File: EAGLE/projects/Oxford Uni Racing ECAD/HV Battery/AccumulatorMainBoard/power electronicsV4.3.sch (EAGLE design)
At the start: 94 parts, among them IC1 4043D, IC2 SE555D, IC9 4011D, K2 T9AS5D12-12=T9A, K3 T9AS1D12-48=T9A, K6 T9AS1D12-48=T9A, K7 T9AS1D12-48=T9A, Q1 BSS138, Q2 BSS138, Q3 BSS138, Q4 BSS138

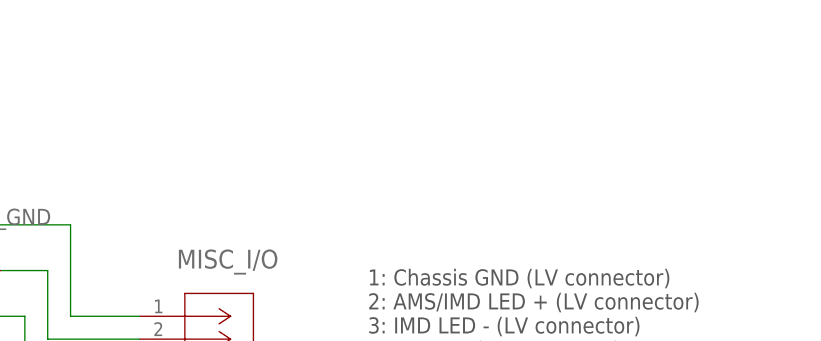
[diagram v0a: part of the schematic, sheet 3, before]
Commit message: main board schematic update with new connectors
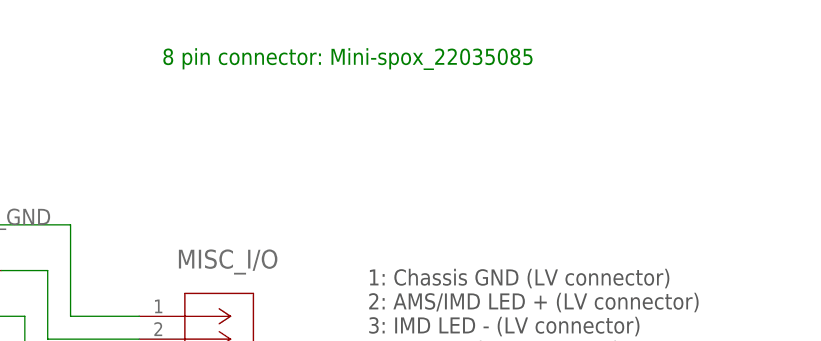
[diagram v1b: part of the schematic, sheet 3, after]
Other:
- note added: "8 pin connector: Mini-spox_22035085"
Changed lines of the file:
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@@
 <grid distance="0.1" unitdist="inch" unit="inch" style="lines" multiple="1" display="no" altdistance="0.01" altunitdist="inch" altunit="inch"/>
 <layers>
-<layer number="1" name="Top" color="4" fill="1" visible="yes" active="no"/>
-<layer number="2" name="Route2" color="16" fill="1" visible="yes" active="no"/>
-<layer number="3" name="Route3" color="17" fill="1" visible="yes" active="no"/>
-<layer number="4" name="Route4" color="18" fill="1" visible="yes" active="no"/>
-<layer number="5" name="Route5" color="19" fill="1" visible="yes" active="no"/>
-<layer number="6" name="Route6" color="25" fill="1" visible="yes" active="no"/>
-<layer number="7" name="Route7" color="26" fill="1" visible="yes" active="no"/>
-<layer number="8" name="Route8" color="27" fill="1" visible="yes" active="no"/>
-<layer number="9" name="Route9" color="28" fill="1" visible="yes" active="no"/>
-<layer number="10" name="Route10" color="29" fill="1" visible="yes" active="no"/>
-<layer number="11" name="Route11" color="30" fill="1" visible="yes" active="no"/>
-<layer number="12" name="Route12" color="20" fill="1" visible="yes" active="no"/>
-<layer number="13" name="Route13" color="21" fill="1" visible="yes" active="no"/>
-<layer number="14" name="Route14" color="22" fill="1" visible="yes" active="no"/>
-<layer number="15" name="Route15" color="23" fill="1" visible="yes" active="no"/>
-<layer number="16" name="Bottom" color="1" fill="1" visible="yes" active="no"/>
-<layer number="17" name="Pads" color="2" fill="1" visible="yes" active="no"/>
-<layer number="18" name="Vias" color="2" fill="1" visible="yes" active="no"/>
-<layer number="19" name="Unrouted" color="6" fill="1" visible="yes" active="no"/>
-<layer number="20" name="Dimension" color="24" fill="1" visible="yes" active="no"/>
-<layer number="21" name="tPlace" color="7" fill="1" visible="yes" active="no"/>
-<layer number="22" name="bPlace" color="7" fill="1" visible="yes" active="no"/>
-<layer number="23" name="tOrigins" color="15" fill="1" visible="yes" active="no"/>
-<layer number="24" name="bOrigins" color="15" fill="1" visible="yes" active="no"/>
-<layer number="25" name="tNames" color="7" fill="1" visible="yes" active="no"/>
-<layer number="26" name="bNames" color="7" fill="1" visible="yes" active="no"/>
-<layer number="27" name="tValues" color="7" fill="1" visible="yes" active="no"/>
-<layer number="28" name="bValues" color="7" fill="1" visible="yes" active="no"/>
+<layer number="1" name="Top" color="4" fill="1" visible="no" active="no"/>
+<layer number="2" name="Route2" color="16" fill="1" visible="no" active="no"/>
+<layer number="3" name="Route3" color="17" fill="1" visible="no" active="no"/>
+<layer number="4" name="Route4" color="18" fill="1" visible="no" active="no"/>
+<layer number="5" name="Route5" color="19" fill="1" visible="no" active="no"/>
+<layer number="6" name="Route6" color="25" fill="1" visible="no" active="no"/>
+<layer number="7" name="Route7" color="26" fill="1" visible="no" active="no"/>
+<layer number="8" name="Route8" color="27" fill="1" visible="no" active="no"/>
+<layer number="9" name="Route9" color="28" fill="1" visible="no" active="no"/>
+<layer number="10" name="Route10" color="29" fill="1" visible="no" active="no"/>
+<layer number="11" name="Route11" color="30" fill="1" visible="no" active="no"/>
+<layer number="12" name="Route12" color="20" fill="1" visible="no" active="no"/>
+<layer number="13" name="Route13" color="21" fill="1" visible="no" active="no"/>
+<layer number="14" name="Route14" color="22" fill="1" visible="no" active="no"/>
+<layer number="15" name="Route15" color="23" fill="1" visible="no" active="no"/>
+<layer number="16" name="Bottom" color="1" fill="1" visible="no" active="no"/>
+<layer number="17" name="Pads" color="2" fill="1" visible="no" active="no"/>
+<layer number="18" name="Vias" color="2" fill="1" visible="no" active="no"/>
+<layer number="19" name="Unrouted" color="6" fill="1" visible="no" active="no"/>
+<layer number="20" name="Dimension" color="24" fill="1" visible="no" active="no"/>
+<layer number="21" name="tPlace" color="7" fill="1" visible="no" active="no"/>
+<layer number="22" name="bPlace" color="7" fill="1" visible="no" active="no"/>
+<layer number="23" name="tOrigins" color="15" fill="1" visible="no" active="no"/>
+<layer number="24" name="bOrigins" color="15" fill="1" visible="no" active="no"/>
+<layer number="25" name="tNames" color="7" fill="1" visible="no" active="no"/>
+<layer number="26" name="bNames" color="7" fill="1" visible="no" active="no"/>
+<layer number="27" name="tValues" color="7" fill="1" visible="no" active="no"/>
+<layer number="28" name="bValues" color="7" fill="1" visible="no" active="no"/>
 <layer number="29" name="tStop" color="7" fill="3" visible="no" active="no"/>
 <layer number="30" name="bStop" color="7" fill="6" visible="no" active="no"/>
@@
 <layer number="35" name="tGlue" color="7" fill="4" visible="no" active="no"/>
 <layer number="36" name="bGlue" color="7" fill="5" visible="no" active="no"/>
-<layer number="37" name="tTest" color="7" fill="1" visible="yes" active="no"/>
-<layer number="38" name="bTest" color="7" fill="1" visible="yes" active="no"/>
+<layer number="37" name="tTest" color="7" fill="1" visible="no" active="no"/>
+<layer number="38" name="bTest" color="7" fill="1" visible="no" active="no"/>
 <layer number="39" name="tKeepout" color="4" fill="11" visible="no" active="no"/>
 <layer number="40" name="bKeepout" color="1" fill="11" visible="no" active="no"/>
@@
 <layer number="44" name="Drills" color="7" fill="1" visible="no" active="no"/>
 <layer number="45" name="Holes" color="7" fill="1" visible="no" active="no"/>
-<layer number="46" name="Milling" color="3" fill="1" visible="yes" active="no"/>
-<layer number="47" name="Measures" color="7" fill="1" visible="yes" active="no"/>
-<layer number="48" name="Document" color="7" fill="1" visible="yes" active="no"/>
-<layer number="49" name="Reference" color="7" fill="1" visible="yes" active="no"/>
-<layer number="50" name="dxf" color="7" fill="1" visible="yes" active="no"/>
-<layer number="51" name="tDocu" color="7" fill="1" visible="yes" active="no"/>
-<layer number="52" name="bDocu" color="7" fill="1" visible="yes" active="no"/>
-<layer number="53" name="tGND_GNDA" color="7" fill="9" visible="yes" active="no"/>
-<layer number="54" name="bGND_GNDA" color="1" fill="9" visible="yes" active="no"/>
-<layer number="56" name="wert" color="7" fill="1" visible="yes" active="no"/>
-<layer number="57" name="tCAD" color="7" fill="1" visible="yes" active="no"/>
-<layer number="59" name="tCarbon" color="7" fill="1" visible="yes" active="no"/>
-<layer number="60" name="bCarbon" color="7" fill="1" visible="yes" active="no"/>
+<layer number="46" name="Milling" color="3" fill="1" visible="no" active="no"/>
+<layer number="47" name="Measures" color="7" fill="1" visible="no" active="no"/>
+<layer number="48" name="Document" color="7" fill="1" visible="no" active="no"/>
+<layer number="49" name="Reference" color="7" fill="1" visible="no" active="no"/>
+<layer number="50" name="dxf" color="7" fill="1" visible="no" active="no"/>
+<layer number="51" name="tDocu" color="7" fill="1" visible="no" active="no"/>
+<layer number="52" name="bDocu" color="7" fill="1" visible="no" active="no"/>
+<layer number="53" name="tGND_GNDA" color="7" fill="9" visible="no" active="no"/>
+<layer number="54" name="bGND_GNDA" color="1" fill="9" visible="no" active="no"/>
+<layer number="56" name="wert" color="7" fill="1" visible="no" active="no"/>
+<layer number="57" name="tCAD" color="7" fill="1" visible="no" active="no"/>
+<layer number="59" name="tCarbon" color="7" fill="1" visible="no" active="no"/>
+<layer number="60" name="bCarbon" color="7" fill="1" visible="no" active="no"/>
 <layer number="88" name="SimResults" color="9" fill="1" visible="yes" active="yes"/>
 <layer number="89" name="SimProbes" color="9" fill="1" visible="yes" active="yes"/>
@@
 3: GND (LV connector)</text>
 <text x="215.9" y="63.5" size="1.778" layer="91">CAN D-sub connector</text>
+<text x="195.58" y="243.84" size="1.778" layer="91">8 pin connector: Mini-spox_22035085</text>
 </plain>
 <instances>

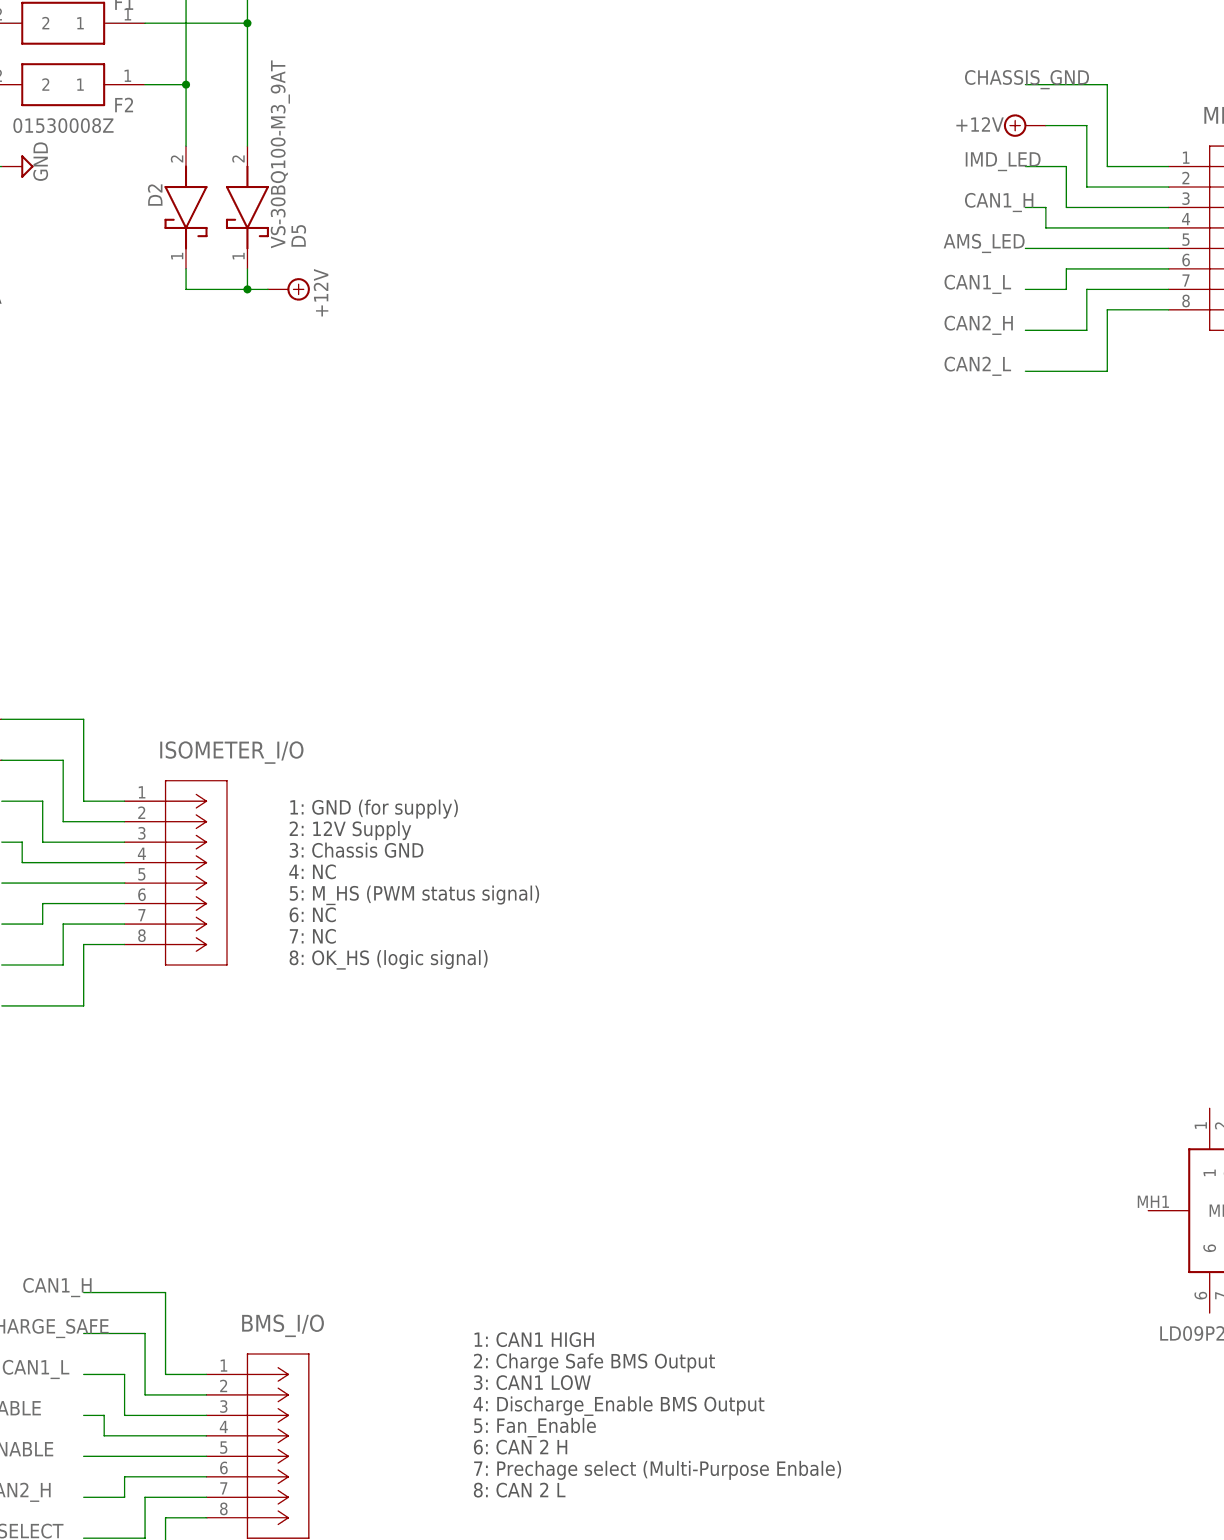
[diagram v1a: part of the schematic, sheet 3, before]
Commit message: Mainboard .brd file updates
Routed all the wires to the connector. and solves DRC conflicts.
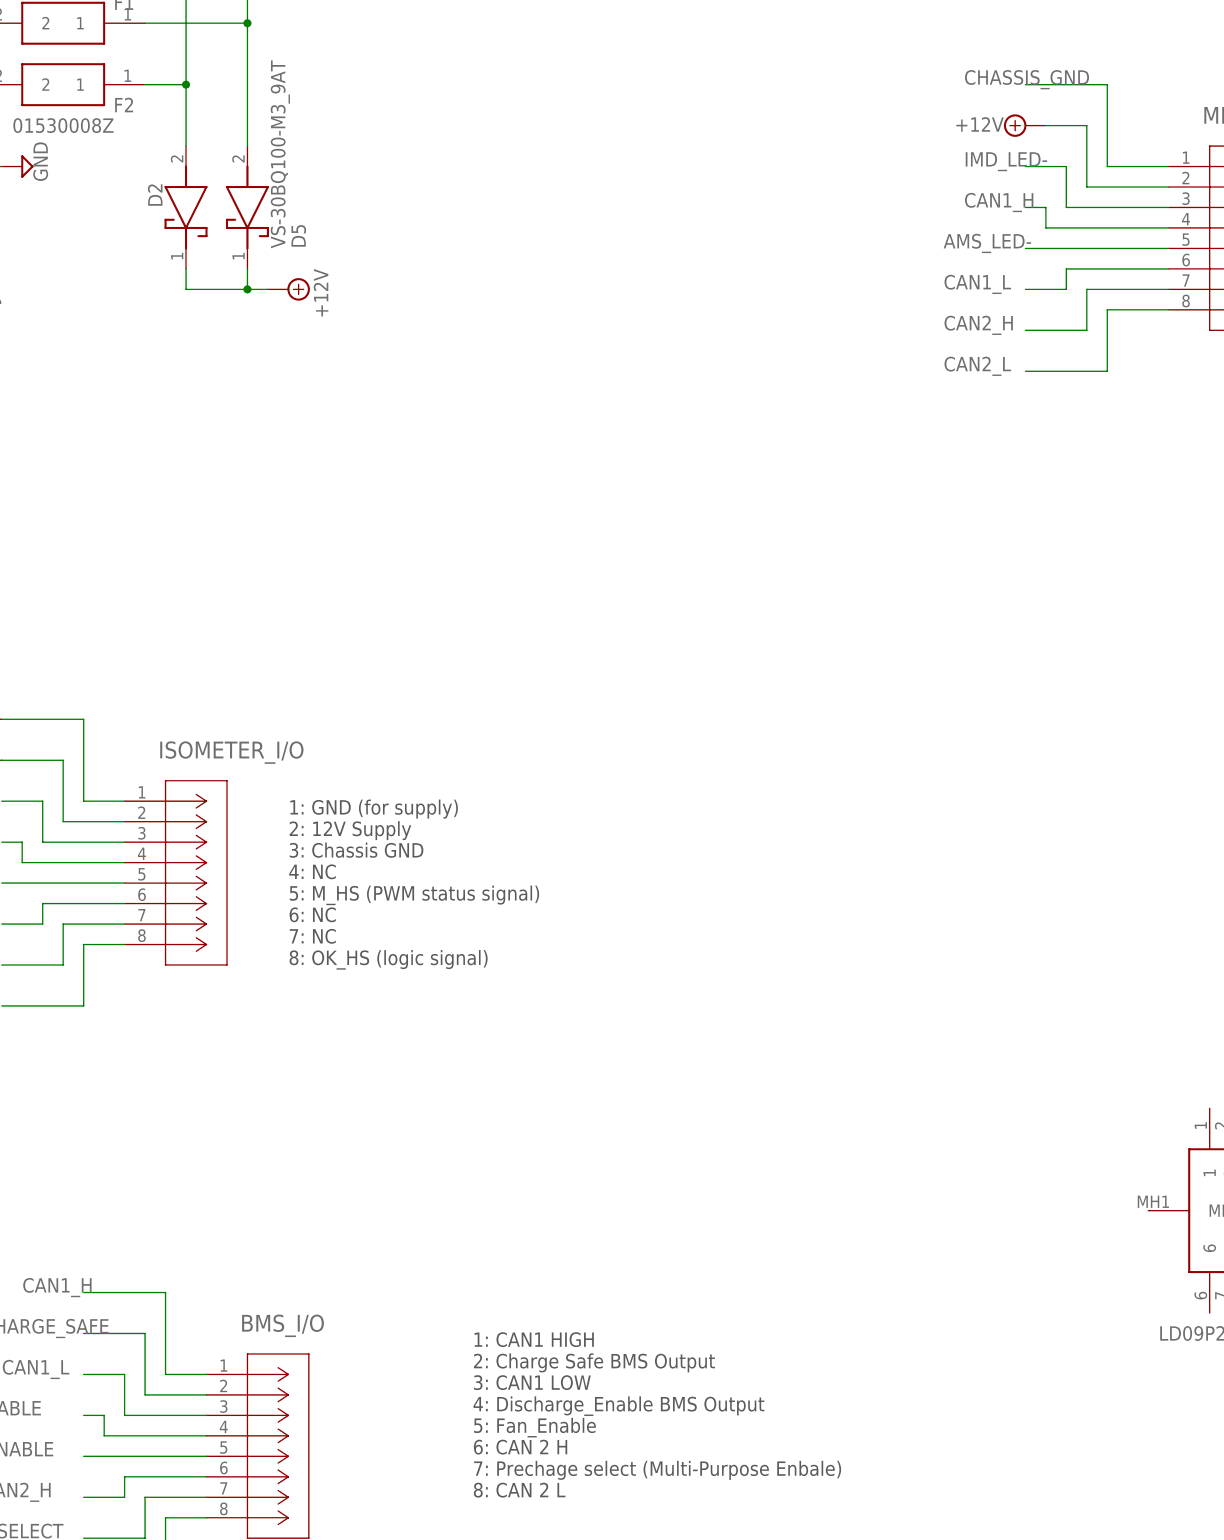
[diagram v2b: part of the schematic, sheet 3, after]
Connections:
- removed net AMS_LED: MISC_I/O.5
- removed net IMD_LED: MISC_I/O.3
- net AMS_LED-: now also MISC_I/O.5
- net IMD_LED-: now also MISC_I/O.3
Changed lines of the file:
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@@
 <net name="CHARGE_SAFE" class="0">
 <segment>
-<pinref part="BMS_I/O" gate="A" pin="2"/>
-<wire x1="73.66" y1="63.5" x2="66.04" y2="63.5" width="0.1524" layer="91"/>
 <wire x1="66.04" y1="63.5" x2="66.04" y2="71.12" width="0.1524" layer="91"/>
 <wire x1="66.04" y1="71.12" x2="58.42" y2="71.12" width="0.1524" layer="91"/>
 <label x="45.72" y="71.12" size="1.778" layer="95"/>
+<pinref part="BMS_I/O" gate="A" pin="2"/>
+<wire x1="66.04" y1="63.5" x2="73.66" y2="63.5" width="0.1524" layer="91"/>
 </segment>
 </net>
@@
 <segment>
 <pinref part="MISC_I/O" gate="A" pin="4"/>
-<wire x1="193.04" y1="208.28" x2="177.8" y2="208.28" width="0.1524" layer="91"/>
 <wire x1="177.8" y1="208.28" x2="177.8" y2="210.82" width="0.1524" layer="91"/>
 <wire x1="177.8" y1="210.82" x2="175.26" y2="210.82" width="0.1524" layer="91"/>
 <label x="167.64" y="210.82" size="1.778" layer="95"/>
+<wire x1="193.04" y1="208.28" x2="177.8" y2="208.28" width="0.1524" layer="91"/>
 </segment>
 <segment>
@@
 </segment>
 </net>
-<net name="IMD_LED" class="0">
+<net name="IMD_LED-" class="0">
 <segment>
 <pinref part="MISC_I/O" gate="A" pin="3"/>
@@
 </segment>
 </net>
-<net name="AMS_LED" class="0">
+<net name="AMS_LED-" class="0">
 <segment>
 <pinref part="MISC_I/O" gate="A" pin="5"/>
